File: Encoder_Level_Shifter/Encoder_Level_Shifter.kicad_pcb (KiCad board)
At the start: 2 copper layers, 17.3 x 11.2 mm, 6 parts, among them J1 Conn_01x04, J2 Conn_01x04

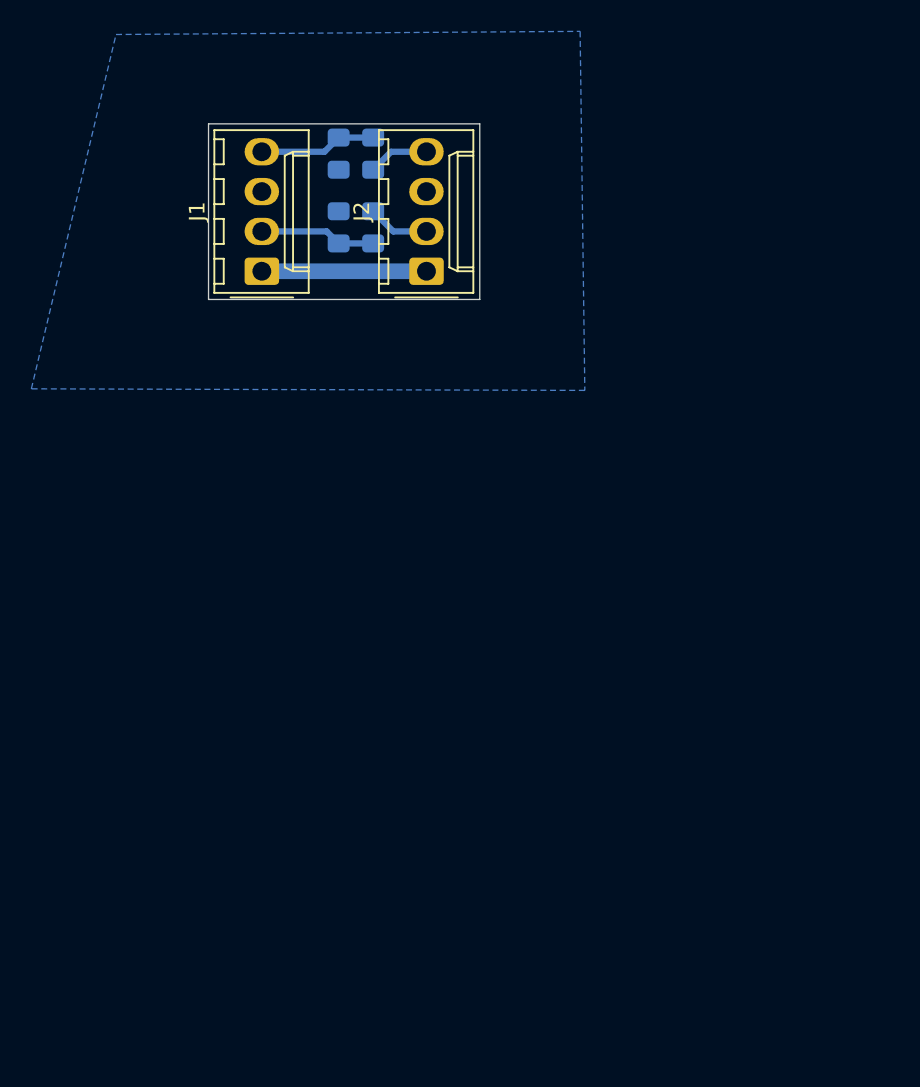
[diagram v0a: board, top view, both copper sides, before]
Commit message: update encoder level shifter
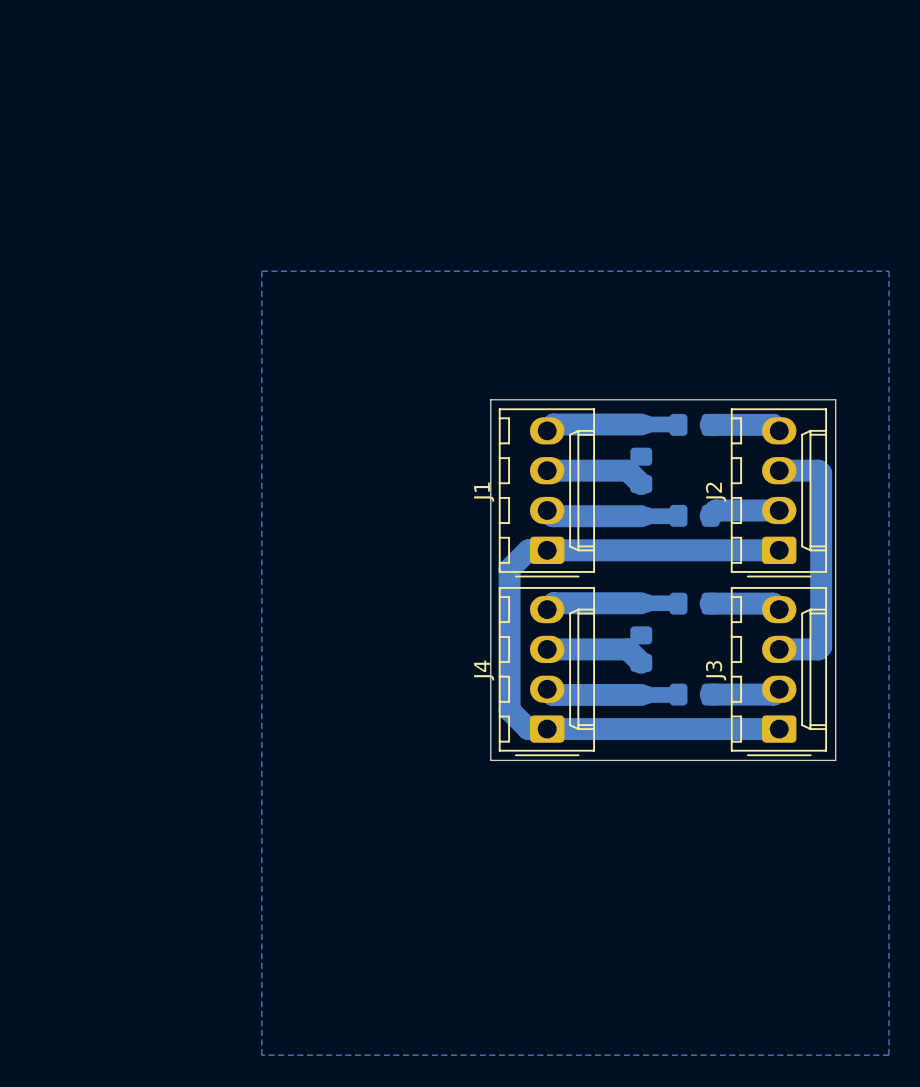
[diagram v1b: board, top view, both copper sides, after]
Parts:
- added J3: Conn_01x04, Connector_Molex:Molex_KK-254_AE-6410-04A_1x04_P2.54mm_Vertical, F.Cu at (133.0, 79.2)
- added J4: Conn_01x04, Connector_Molex:Molex_KK-254_AE-6410-04A_1x04_P2.54mm_Vertical, F.Cu at (118.2, 79.2)
- added R5: 10k, Resistor_SMD:R_0805_2012Metric_Pad1.15x1.40mm_HandSolder, B.Cu at (124.2, 72.2)
- added R6: 10k, Resistor_SMD:R_0805_2012Metric_Pad1.15x1.40mm_HandSolder, B.Cu at (124.2, 76.0)
- added R7: 5.4k, Resistor_SMD:R_0805_2012Metric_Pad1.15x1.40mm_HandSolder, B.Cu at (127.6, 71.2)
- added R8: 5.4k, Resistor_SMD:R_0805_2012Metric_Pad1.15x1.40mm_HandSolder, B.Cu at (127.6, 77.0)
- moved J2 28.7 mm to (133.0, 67.8)
- moved R4 27.5 mm to (127.6, 65.6), turned to 180 degrees
- moved R3 26.8 mm to (127.6, 59.8), turned to 180 degrees
- moved R1 26.6 mm to (124.2, 60.8)
- moved R2 26.0 mm to (124.2, 64.6)
- moved J1 25.5 mm to (118.2, 67.8)
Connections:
- net /A_In renamed Net-(J2-Pad2)
- net /A_Out renamed Net-(J1-Pad2)
- net /B_In renamed Net-(J2-Pad4)
- net /B_Out renamed Net-(J1-Pad4)
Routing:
- net +5V: track 10.5 -> 44.4 mm
- net GND: track 0.00 -> 29.3 mm
- net Net-(J4-Pad4): track 0.00 -> 8.55 mm
- net Net-(J4-Pad2): track 0.00 -> 8.54 mm
- net Net-(J3-Pad4): track 0.00 -> 4.53 mm
- net Net-(J3-Pad2): track 0.00 -> 4.52 mm
- net Net-(J1-Pad2): track 7.42 -> 8.54 mm
- net Net-(J1-Pad4): track 7.47 -> 8.55 mm
- net Net-(J2-Pad4): track 3.87 -> 4.53 mm
- net Net-(J2-Pad2): track 3.93 -> 4.52 mm
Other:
- board size 17.3 x 11.2 mm -> 22 x 23 mm
